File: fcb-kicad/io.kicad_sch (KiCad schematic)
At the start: 14 parts, among them J4 USB_B_Micro, J5 Conn_01x01_Female, J6 Conn_01x01_Female, Q1 S8050 J3Y, SW3 SW_SPST, U9 USBLC6-2SC6

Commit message: 4in1 connector library part, SPI CS pullups, migrate magnetometer cirtuit
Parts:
- gave numbers to parts that had none: 1
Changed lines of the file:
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@@
   (symbol (lib_id "Device:LED") (at 88.9 116.84 90) (unit 1)
     (in_bom yes) (on_board yes) (fields_autoplaced)
-    (property "Reference" "D?" (id 0) (at 91.821 117.519 90)
+    (property "Reference" "D6" (id 0) (at 91.821 117.519 90)
       (effects (font (size 1.27 1.27)) (justify right))
     )

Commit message: buzzer notes
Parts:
- BZ1: footprint Buzzer_Beeper:Buzzer_TDK_PS1240P02BT_D12.2mm_H6.5mm -> 000_sjt:MLT-8350
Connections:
- net +5V is gone; now on net +3V3: BZ1.1 (-), D7.1 (K)
- net Q_buzzer_B: now reaches Q1.1 (B), R18.2
- net Q_buzzzer_C: now reaches BZ1.2 (+), D7.2 (A), Q1.3 (C)
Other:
- note added: "(3.3-0.6) V / 16 Ω ≈ 170 mA"
- note added: "600 mV @ 500 mA"
- note added: "~16Ω"
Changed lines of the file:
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@@
   (junction (at 58.42 110.49) (diameter 0) (color 0 0 0 0)
+  )
+  (junction (at 120.015 57.15) (diameter 0) (color 0 0 0 0)
   )
   (junction (at 130.81 45.72) (diameter 0) (color 0 0 0 0)
@@
   (no_connect (at 29.845 54.61))
   (no_connect (at 19.685 59.69))
+  (wire (pts (xy 120.015 57.15) (xy 123.19 57.15))
+    (stroke (width 0) (type default) (color 0 0 0 0))
+  )
   (wire (pts (xy 78.105 52.07) (xy 70.485 52.07))
     (stroke (width 0) (type default) (color 0 0 0 0))
@@
     (stroke (width 0) (type default) (color 0 0 0 0))
   )
+  (wire (pts (xy 120.015 57.15) (xy 120.015 61.595))
+    (stroke (width 0) (type default) (color 0 0 0 0))
+  )
   (wire (pts (xy 130.81 39.37) (xy 133.35 39.37))
     (stroke (width 0) (type default) (color 0 0 0 0))
@@
     (stroke (width 0) (type default) (color 0 0 0 0))
   )
-  (wire (pts (xy 119.38 57.15) (xy 123.19 57.15))
+  (wire (pts (xy 119.38 57.15) (xy 120.015 57.15))
     (stroke (width 0) (type default) (color 0 0 0 0))
   )
@@
   )
   (text "TVS protection" (at 43.815 46.355 0)
+    (effects (font (size 1.27 1.27)) (justify left bottom))
+  )
+  (text "~16Ω" (at 139.065 38.735 0)
+    (effects (font (size 1.27 1.27)) (justify left bottom))
+  )
+  (text "600 mV @ 500 mA" (at 133.985 62.23 0)
+    (effects (font (size 1.27 1.27)) (justify left bottom))
+  )
+  (text "(3.3-0.6) V / 16 Ω ≈ 170 mA" (at 94.615 33.655 0)
+    (effects (font (size 1.27 1.27)) (justify left bottom))
+  )
+  (label "Q_buzzer_B" (at 120.015 61.595 180)
+    (effects (font (size 1.27 1.27)) (justify right bottom))
+  )
+  (label "Q_buzzzer_C" (at 130.81 49.53 0)
     (effects (font (size 1.27 1.27)) (justify left bottom))
   )
@@
     (pin "1")
   )
-  (symbol (lib_id "power:+5V") (at 130.81 34.29 0) (unit 1)
-    (in_bom yes) (on_board yes) (fields_autoplaced)
-    (property "Reference" "#PWR036" (id 0) (at 130.81 38.1 0)
-      (effects (font (size 1.27 1.27)) hide)
-    )
-    (property "Value" "+5V" (id 1) (at 130.81 30.6855 0))
+  (symbol (lib_id "power:+3V3") (at 130.81 34.29 0) (unit 1)
+    (in_bom yes) (on_board yes) (fields_autoplaced)
+    (property "Reference" "#PWR?" (id 0) (at 130.81 38.1 0)
+      (effects (font (size 1.27 1.27)) hide)
+    )
+    (property "Value" "+3V3" (id 1) (at 130.81 30.6855 0))
     (property "Footprint" "" (id 2) (at 130.81 34.29 0)
       (effects (font (size 1.27 1.27)) hide)
@@
       (effects (font (size 1.27 1.27)) (justify left))
     )
-    (property "Footprint" "Buzzer_Beeper:Buzzer_TDK_PS1240P02BT_D12.2mm_H6.5mm" (id 2) (at 135.255 39.37 90)
-      (effects (font (size 1.27 1.27)) hide)
-    )
+    (property "Footprint" "000_sjt:MLT-8350" (id 2) (at 135.255 39.37 90)
+      (effects (font (size 1.27 1.27)) hide)
+    )

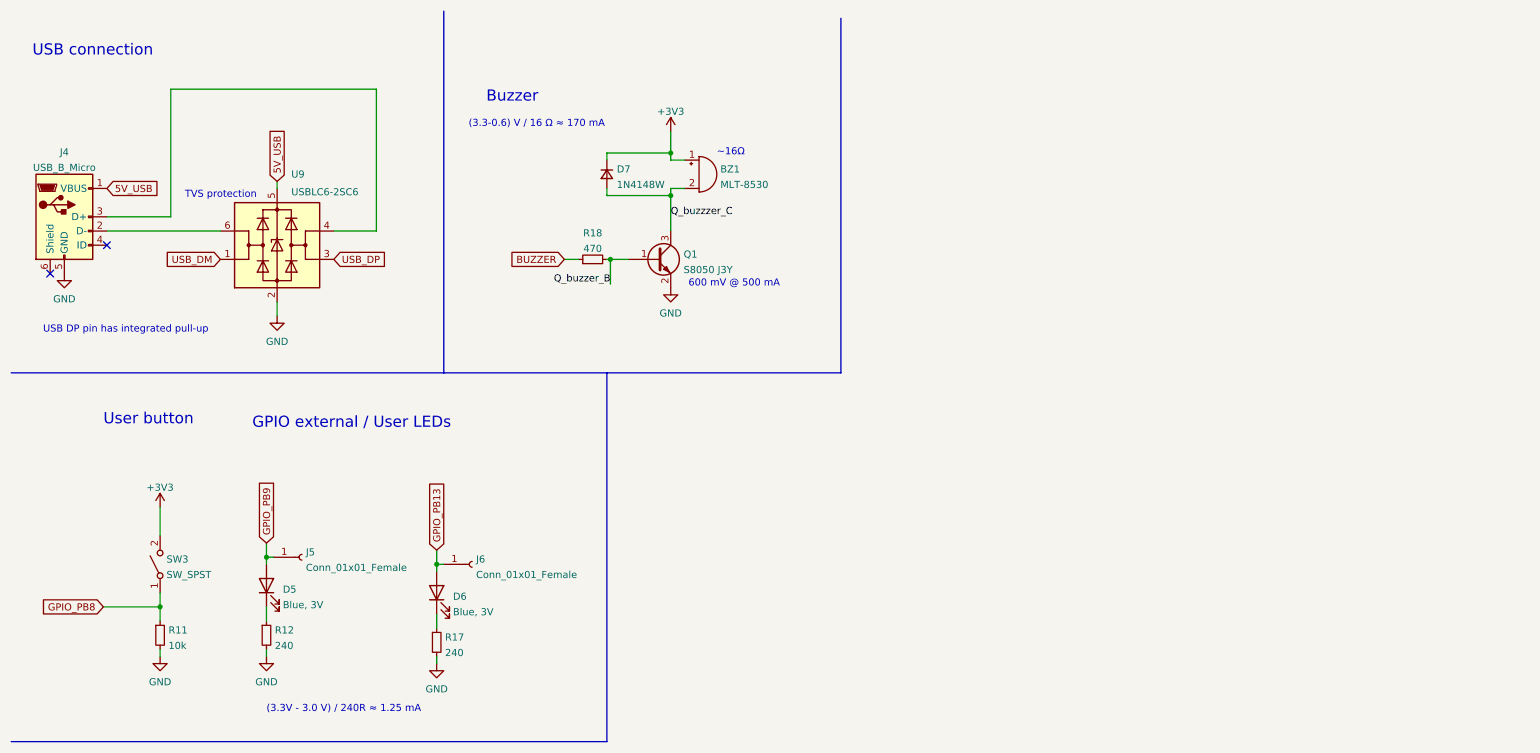
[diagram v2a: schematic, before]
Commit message: Analog inputs, connectors to GPIO
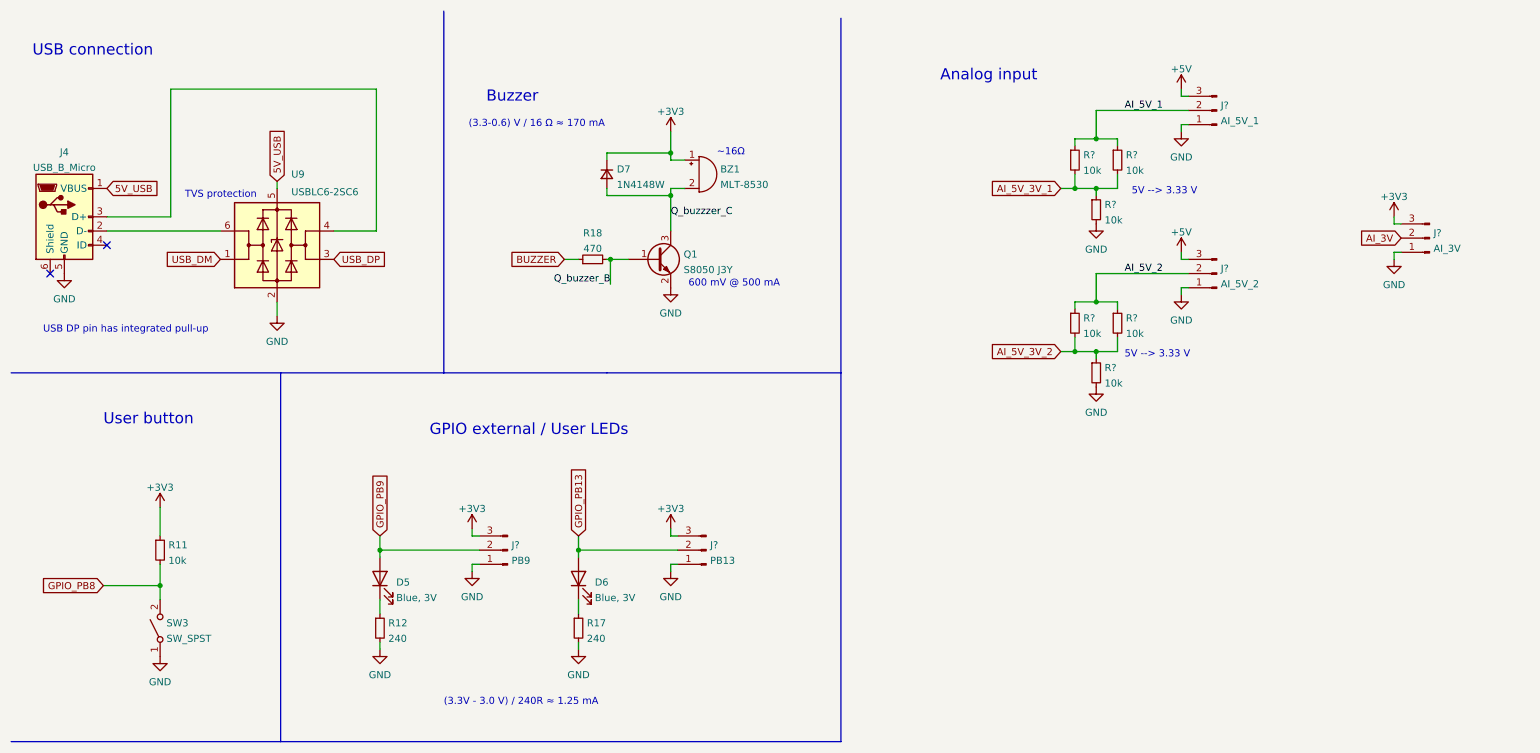
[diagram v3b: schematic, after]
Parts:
- removed J5, J6: Conn_01x01_Female, symbol Connector:Conn_01x01_Female
- added J?: PB13, symbol Connector:Conn_01x03_Male
- added J?: AI_5V_1, symbol Connector:Conn_01x03_Male
- added J?: AI_3V, symbol Connector:Conn_01x03_Male
- added J?: AI_5V_2, symbol Connector:Conn_01x03_Male
- added J?: PB9, symbol Connector:Conn_01x03_Male
- added R? (x6): 10k, symbol Device:R_Small
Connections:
- net +3V3: now also R11.1, J?.3 (Pin_3), J?.3 (Pin_3), J?.3 (Pin_3); no longer SW3.2 (B)
- net GND: now also SW3.1 (A), J?.1 (Pin_1), J?.1 (Pin_1), J?.1 (Pin_1), J?.1 (Pin_1), J?.1 (Pin_1), R?.2, R?.2; no longer R11.2
- net GPIO_PB13: now also J?.2 (Pin_2)
- net GPIO_PB8: now also R11.2, SW3.2 (B); no longer R11.1, SW3.1 (A)
- net GPIO_PB9: now also J?.2 (Pin_2)
- new net +5V: J?.3 (Pin_3), J?.3 (Pin_3)
- new net AI_3V: J?.2 (Pin_2)
- new net AI_5V_1: J?.2 (Pin_2), R?.1, R?.1
- new net AI_5V_2: J?.2 (Pin_2), R?.1, R?.1
- new net AI_5V_3V_1: R?.1, R?.2, R?.2
- new net AI_5V_3V_2: R?.1, R?.2, R?.2
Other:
- note added: "5V --> 3.33 V"
- note added: "Analog input"
- moved on the sheet: D5, D6, R11, R12, R17, SW3

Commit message: Schema rev0 done, Layout components grouped
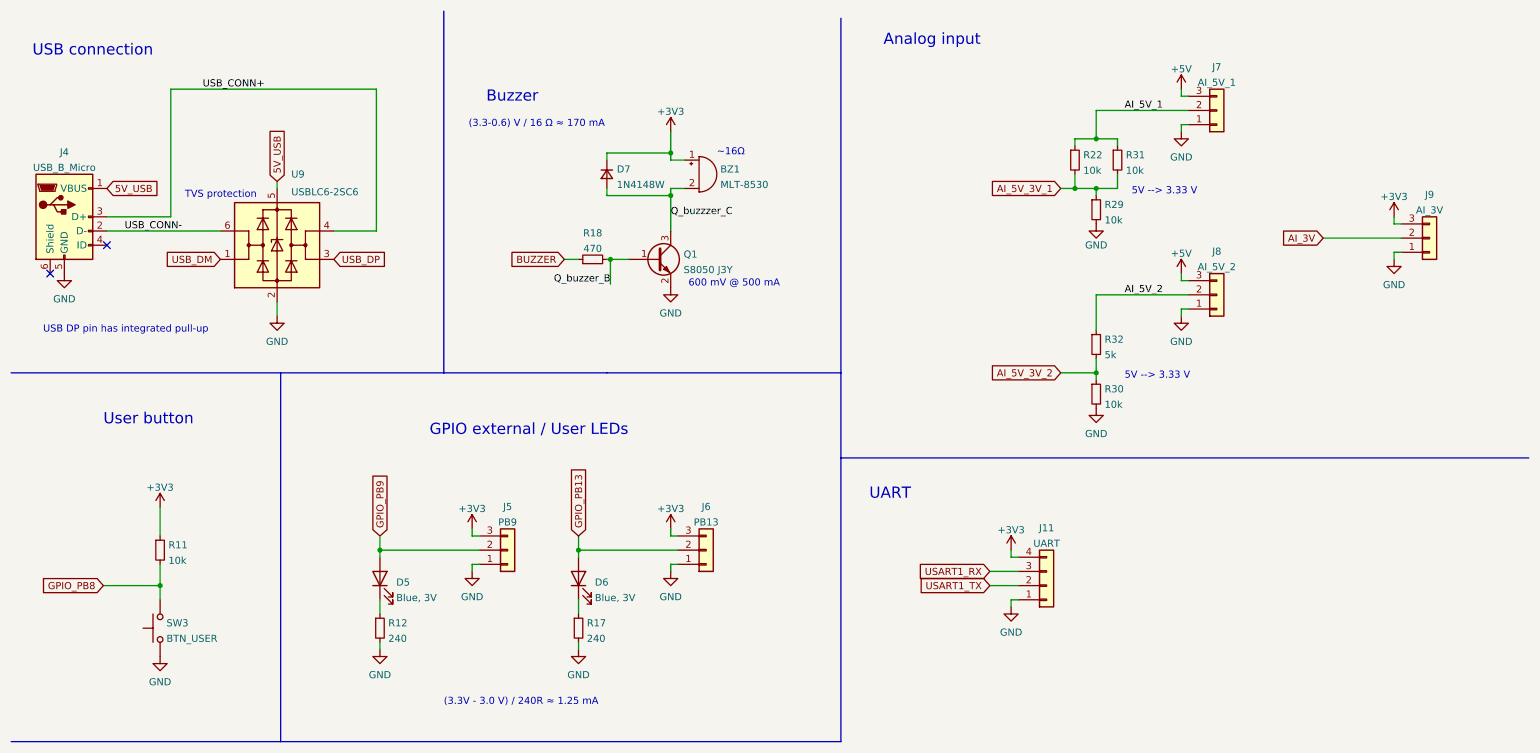
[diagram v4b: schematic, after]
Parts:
- removed R?: 10k, symbol Device:R_Small
- removed SW3: SW_SPST, symbol Switch:SW_SPST
- added J11: UART, Connector_PinHeader_2.00mm:PinHeader_1x04_P2.00mm_Vertical, symbol Connector_Generic:Conn_01x04
- added SW3: BTN_USER, 000_sjt:Button-2.9x4.0mm-SMD, symbol Switch:SW_Push
- J4: footprint (none) -> 000_omat:MICRO-USB-SMD_U254-051T-4BH83-F1S
- J5, J6, J7, J8, J9: renamed from J?; footprint (none) -> Connector_PinHeader_2.00mm:PinHeader_1x03_P2.00mm_Vertical; symbol Connector:Conn_01x03_Male -> Connector_Generic:Conn_01x03
- R22, R29, R30, R31: renamed from R?; footprint (none) -> Resistor_SMD:R_0603_1608Metric
- R32: renamed from R?; value 10k -> 5k; footprint (none) -> Resistor_SMD:R_0603_1608Metric
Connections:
- net +3V3: now also J11.4 (Pin_4)
- net GND: now also J11.1 (Pin_1), SW3.1
- net GPIO_PB8: now also SW3.2
- net USB_CONN-: now reaches J4.2 (D-), U9.6 (I/O1)
- net USB_CONN+: now reaches J4.3 (D+), U9.4 (I/O2)
- new net USART1_RX: J11.3 (Pin_3)
- new net USART1_TX: J11.2 (Pin_2)
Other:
- note added: "UART"
- title: GPIO, Analog inputs -> USB, Buzzer, GPIO, Analog, UART
- moved on the sheet: R30, R32

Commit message: PCB rev0: "Babby's first Leiska"
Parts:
- removed R22: 10k, Resistor_SMD:R_0603_1608Metric, symbol Device:R_Small
- J5: renamed from J4; footprint 000_omat:MICRO-USB-SMD_U254-051T-4BH83-F1S -> 000_sjt:MICRO-USB-SMD_U254-051T-4BH83-F1S
- R27: renamed from R31; value 10k -> 5k
- renumbered J8 to J10, J9 to J11, J5 to J6, J6 to J7, J11 to J8, J7 to J9, R11 to R23, R12 to R24, R17 to R25, R18 to R26, R29 to R28, R32 to R29
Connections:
- net USB_DM renamed USB_D-
- net USB_DP renamed USB_D+
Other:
- moved on the sheet: R27

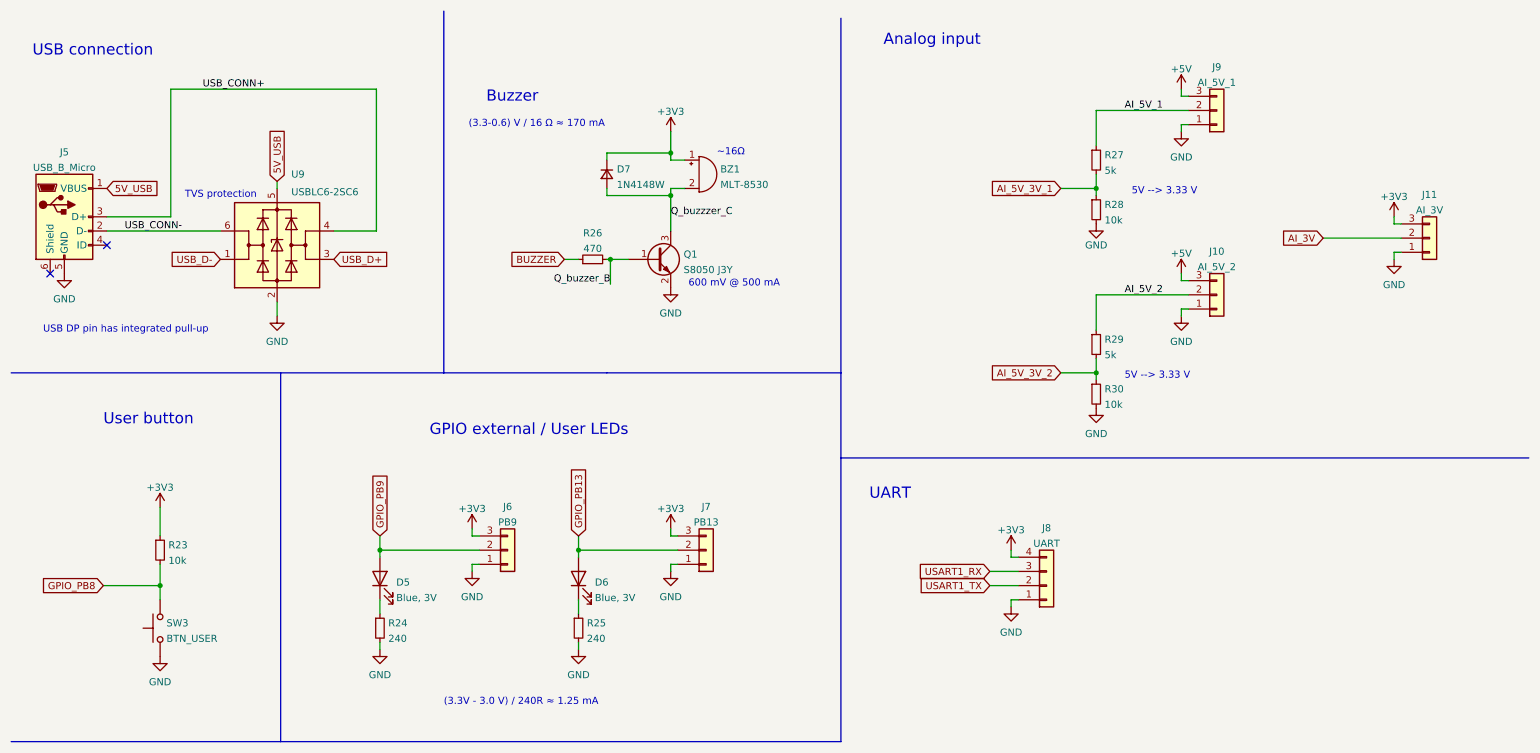
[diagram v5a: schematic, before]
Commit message: Less routing on inner layers, fabrication, BOM should be OK
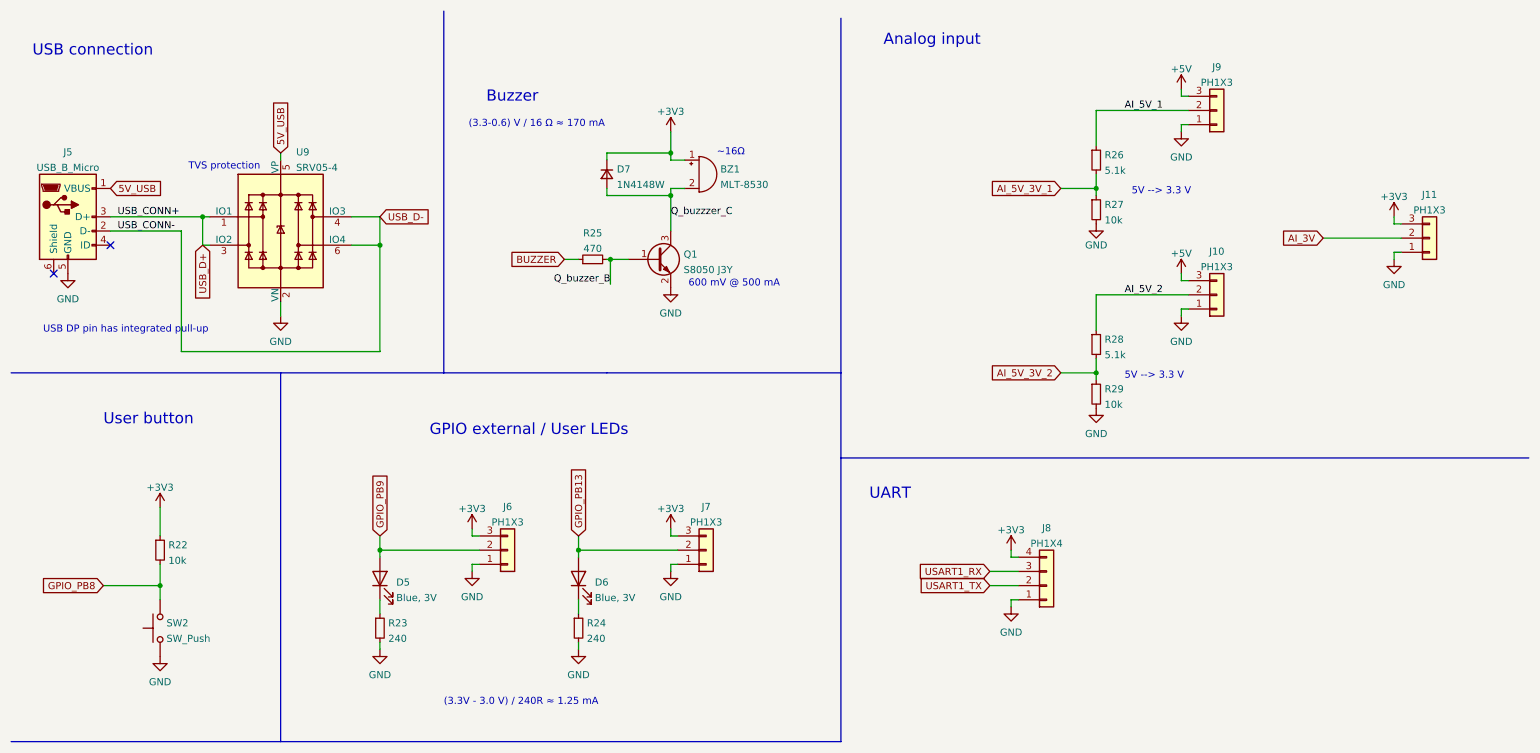
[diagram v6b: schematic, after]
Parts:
- removed U9: USBLC6-2SC6, Package_TO_SOT_SMD:SOT-23-6, symbol Power_Protection:USBLC6-2SC6
- added U9: SRV05-4, Package_TO_SOT_SMD:SOT-23-6, symbol Power_Protection:SRV05-4
- J10: value AI_5V_2 -> PH1X3; LCSC (none) -> C571312
- J11: value AI_3V -> PH1X3; LCSC (none) -> C571312
- J5: LCSC (none) -> C397452
- J6: value PB9 -> PH1X3; LCSC (none) -> C571312
- J7: value PB13 -> PH1X3; LCSC (none) -> C571312
- J8: value UART -> PH1X4; LCSC (none) -> C388723
- J9: value AI_5V_1 -> PH1X3; LCSC (none) -> C571312
- R26: renamed from R27; value 5k -> 5.1k; LCSC (none) -> C23186
- R27: renamed from R28; LCSC (none) -> C25804
- R28: renamed from R29; value 5k -> 5.1k; LCSC (none) -> C23186
- R29: renamed from R30; LCSC (none) -> C25804
- SW2: renamed from SW3; value BTN_USER -> SW_Push
- renumbered R23 to R22, R24 to R23, R25 to R24, R26 to R25
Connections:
- net USB_CONN+ is gone; now on net USB_D+: J5.3 (D+)
- net USB_CONN- is gone; now on net USB_D-: J5.2 (D-)
- net 5V_USB: now also U9.5 (VP)
- net GND: now also U9.2 (VN)
- net USB_D+: now also U9.1 (IO1), U9.3 (IO2)
- net USB_D-: now also U9.4 (IO3), U9.6 (IO4)
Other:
- note added: "5V --> 3.3 V"
- note removed: "5V --> 3.33 V"
- moved on the sheet: J5
